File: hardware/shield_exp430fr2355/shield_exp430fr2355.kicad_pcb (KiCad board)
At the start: 2 copper layers, 78.4 x 50 mm, 50 parts, among them J1 TI_BOOSTER_40_J1, J10 Conn_01x02_Male, J12 Conn_01x02_Male, J13 Conn_01x02_Male, J14 Conn_01x02_Male, J15 Conn_01x02_Male, J16 Conn_01x02_Male, J17 Conn_01x02_Male, J18 Conn_01x02_Male, J19 Conn_01x02_Male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

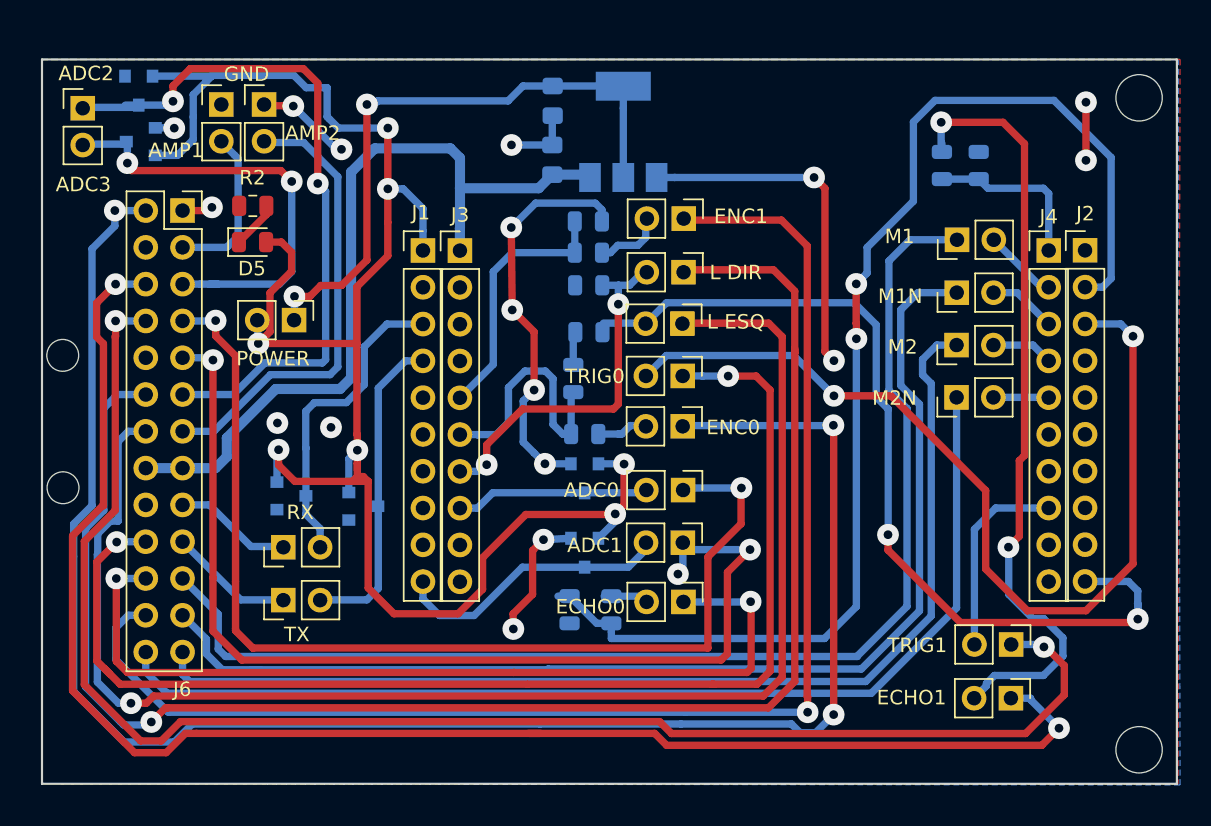
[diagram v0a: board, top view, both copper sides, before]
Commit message: Adicionado exemplo do ADC com trigger por timer.
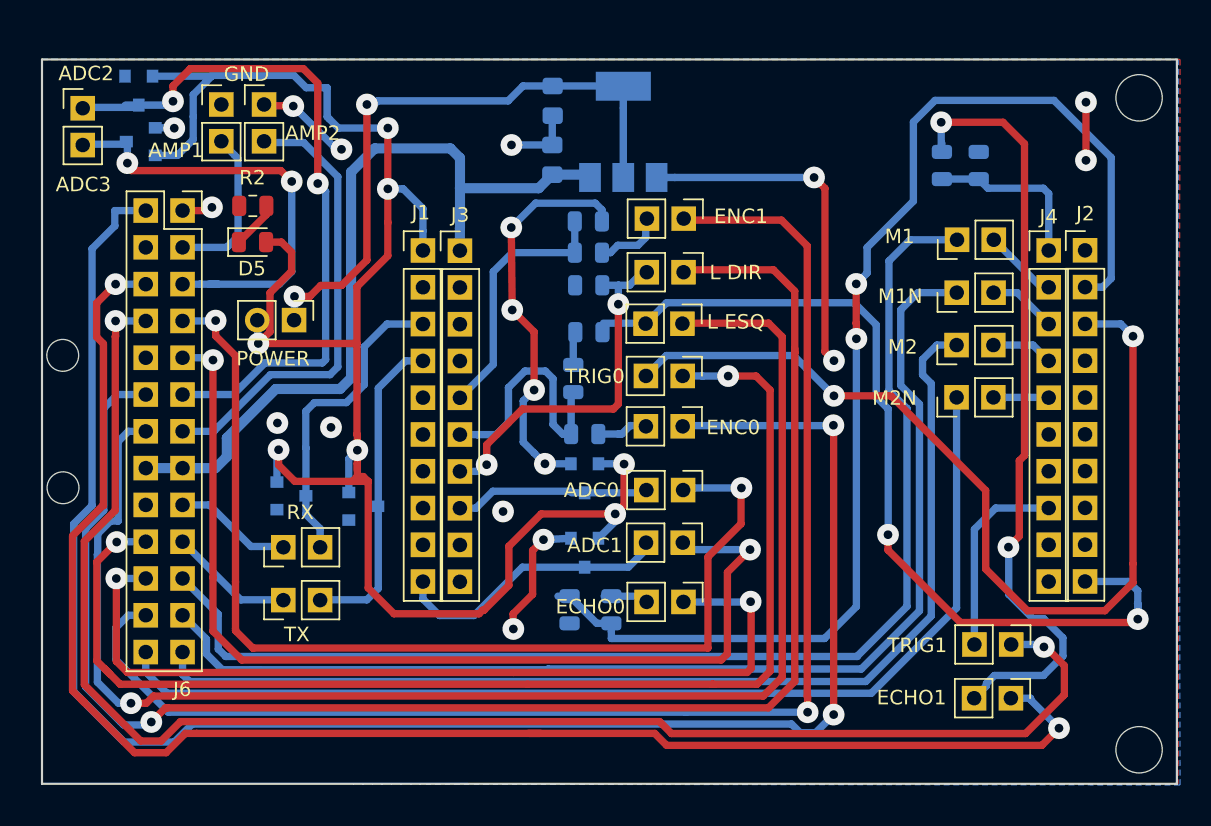
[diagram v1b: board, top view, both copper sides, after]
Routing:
- net ADC1: track 71.7 -> 69.9 mm, vias 3 -> 2
- net P2.2: track 65.4 -> 66.2 mm
- net D0: track 122.1 -> 122.0 mm, vias 3 -> 2
- net GND: vias 17 -> 18

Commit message: Added aligment info
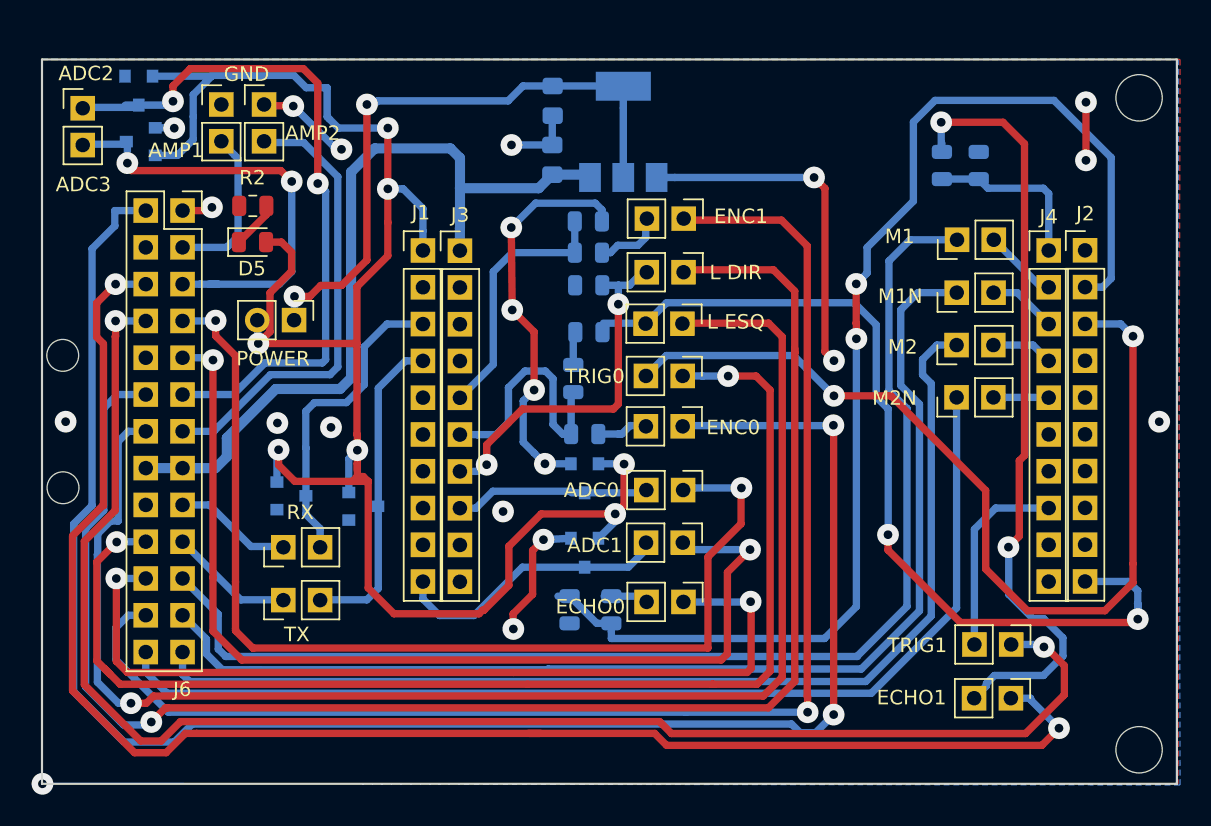
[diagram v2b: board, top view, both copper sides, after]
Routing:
- net GND: vias 18 -> 20
- net (no net): vias 0 -> 1
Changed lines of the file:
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@@
   (general
     (thickness 1.6)
-    (drawings 28)
-    (tracks 626)
+    (drawings 31)
+    (tracks 629)
     (zones 0)
     (modules 50)
@@
     (pad_to_mask_clearance 0)
     (solder_mask_min_width 0.25)
-    (aux_axis_origin 0 0)
+    (aux_axis_origin 171.1 172.9)
     (visible_elements 7FFFFFFF)
     (pcbplotparams
@@
       (padsonsilk false)
       (subtractmaskfromsilk false)
-      (outputformat 3)
+      (outputformat 1)
       (mirror false)
       (drillshape 0)
@@
     )
   )
+  (target plus (at 172.7 147.9) (size 2) (width 0.14986) (layer Edge.Cuts))
+  (target plus (at 248.2 147.9) (size 2) (width 0.14986) (layer Edge.Cuts))
+  (dimension 25.000799 (width 0.25) (layer F.SilkS)
+    (gr_text "25.001 mm" (at 261.2 135.400399 270) (layer F.SilkS)
+      (effects (font (size 1 1) (thickness 0.25)))
+    )
+    (feature1 (pts (xy 249.4 147.900799) (xy 260.286421 147.900799)))
+    (feature2 (pts (xy 249.4 122.9) (xy 260.286421 122.9)))
+    (crossbar (pts (xy 259.7 122.9) (xy 259.7 147.900799)))
+    (arrow1a (pts (xy 259.7 147.900799) (xy 259.113579 146.774295)))
+    (arrow1b (pts (xy 259.7 147.900799) (xy 260.286421 146.774295)))
+    (arrow2a (pts (xy 259.7 122.9) (xy 259.113579 124.026504)))
+    (arrow2b (pts (xy 259.7 122.9) (xy 260.286421 124.026504)))
+  )
+  (dimension 50.000899 (width 0.25) (layer F.SilkS)
+    (gr_text "50.001 mm" (at 256.3 147.900449 270) (layer F.SilkS)
+      (effects (font (size 1 1) (thickness 0.25)))
+    )
+    (feature1 (pts (xy 249.4 172.900899) (xy 255.386421 172.900899)))
+    (feature2 (pts (xy 249.4 122.9) (xy 255.386421 122.9)))
+    (crossbar (pts (xy 254.8 122.9) (xy 254.8 172.900899)))
+    (arrow1a (pts (xy 254.8 172.900899) (xy 254.213579 171.774395)))
+    (arrow1b (pts (xy 254.8 172.900899) (xy 255.386421 171.774395)))
+    (arrow2a (pts (xy 254.8 122.9) (xy 254.213579 124.026504)))
+    (arrow2b (pts (xy 254.8 122.9) (xy 255.386421 124.026504)))
+  )
   (gr_text M2N (at 229.92 146.27) (layer F.SilkS)
     (effects (font (size 1 1) (thickness 0.1)))
@@
     (arrow2b (pts (xy 189.765054 122.89217) (xy 190.351474 124.018673)))
   )
-  (dimension 50.8 (width 0.25) (layer Dwgs.User)
-    (gr_text "2.0000 in" (at 220.245053 115.542172) (layer Dwgs.User)
-      (effects (font (size 1 1) (thickness 0.25)))
-    )
-    (feature1 (pts (xy 245.645053 122.89217) (xy 245.645053 114.542172)))
-    (feature2 (pts (xy 194.845053 122.89217) (xy 194.845053 114.542172)))
-    (crossbar (pts (xy 194.845053 116.542172) (xy 245.645053 116.542172)))
-    (arrow1a (pts (xy 245.645053 116.542172) (xy 244.51855 117.128592)))
-    (arrow1b (pts (xy 245.645053 116.542172) (xy 244.51855 115.955752)))
-    (arrow2a (pts (xy 194.845053 116.542172) (xy 195.971556 117.128592)))
-    (arrow2b (pts (xy 194.845053 116.542172) (xy 195.971556 115.955752)))
-  )
   (gr_line (start 171.069 172.8978) (end 171.069 122.8852) (angle 90) (layer Edge.Cuts) (width 0.14986))
   (gr_line (start 249.42 122.90217) (end 249.42 172.9) (angle 90) (layer Edge.Cuts) (width 0.14986))
+  (via (at 171.1 172.9) (size 1.5) (drill 0.6) (layers F.Cu B.Cu) (net 0))
   (via (at 180.1996 127.635) (size 1.5) (drill 0.6) (layers F.Cu B.Cu) (net 1))
   (segment (start 178.8889 127.6121) (end 180.1767 127.6121) (width 0.508) (layer B.Cu) (net 1))
@@
   (segment (start 205.7908 150.8064) (end 205.2762 150.8064) (width 0.508) (layer F.Cu) (net 1))
   (via (at 205.7908 150.8064) (size 1.5) (drill 0.6) (layers F.Cu B.Cu) (net 1))
+  (via (at 172.7 147.9) (size 1.5) (drill 0.6) (layers F.Cu B.Cu) (net 1))
+  (via (at 248.2 147.9) (size 1.5) (drill 0.6) (layers F.Cu B.Cu) (net 1))
   (segment (start 205.36103 131.78217) (end 206.2988 130.8444) (width 0.7) (layer B.Cu) (net 2))
   (segment (start 199.925053 131.78217) (end 205.36103 131.78217) (width 0.7) (layer B.Cu) (net 2))

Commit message: Updated FR2553 PCB. Vias are now 1.8mm
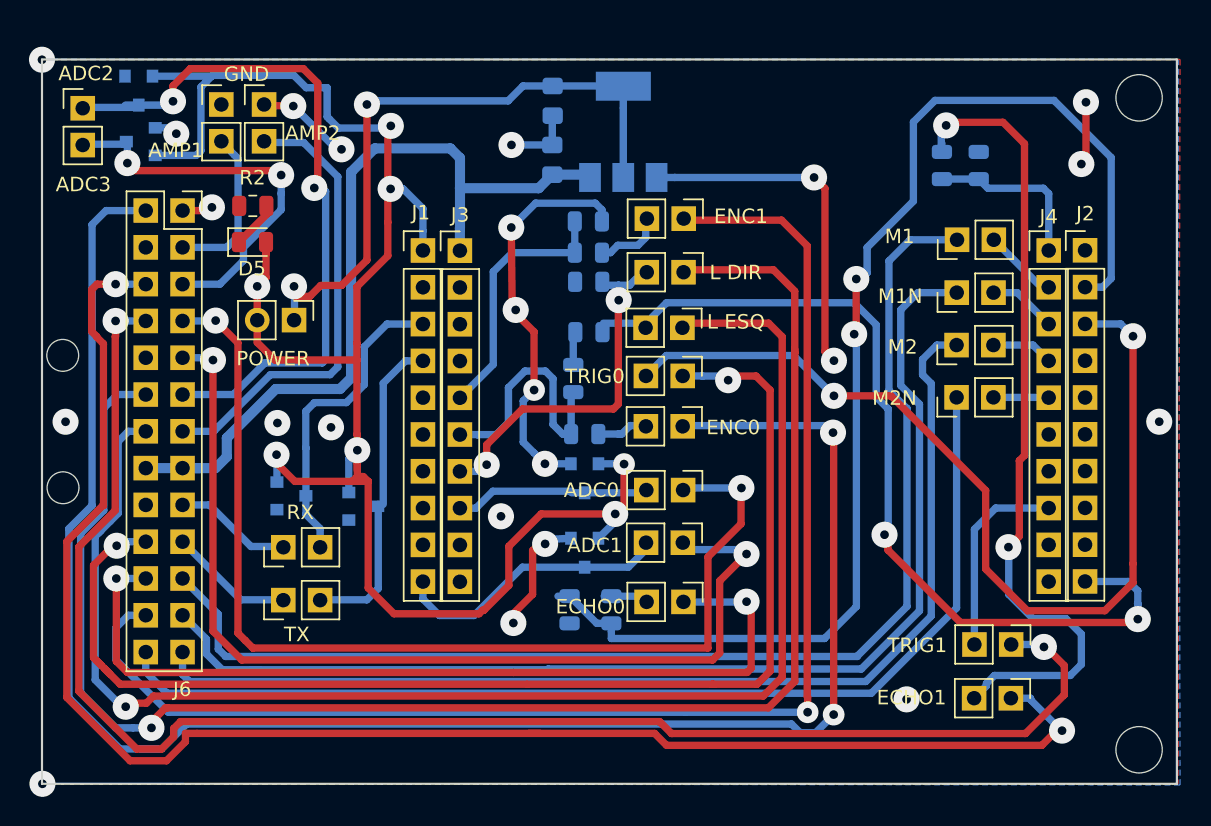
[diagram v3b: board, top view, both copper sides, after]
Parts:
- moved J25 0.28 mm to (215.3, 141.4)
- moved R8 0.24 mm to (208.8, 138.2)
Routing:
- net ADC3: track 31.3 -> 27.4 mm
- net Net-(J19-Pad2): track 54.3 -> 57.3 mm
- net Echo1: track 108.5 -> 110.8 mm
- net Trig1: track 105.5 -> 107.1 mm
- net +3V3: track 128.2 -> 126.6 mm
- net D0: track 122.0 -> 123.5 mm
- net R_TCRT: track 110.0 -> 111.0 mm
- net ADC1: track 69.9 -> 69.1 mm
- net Trig0: track 84.8 -> 85.4 mm
- net (no net): vias 1 -> 3
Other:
- net class +5V: via_dia 1.5 -> 1.8
- net class Default: via_dia 1.5 -> 1.8

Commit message: Updated FR2553 PCB. Connector pads are now 2x2mm
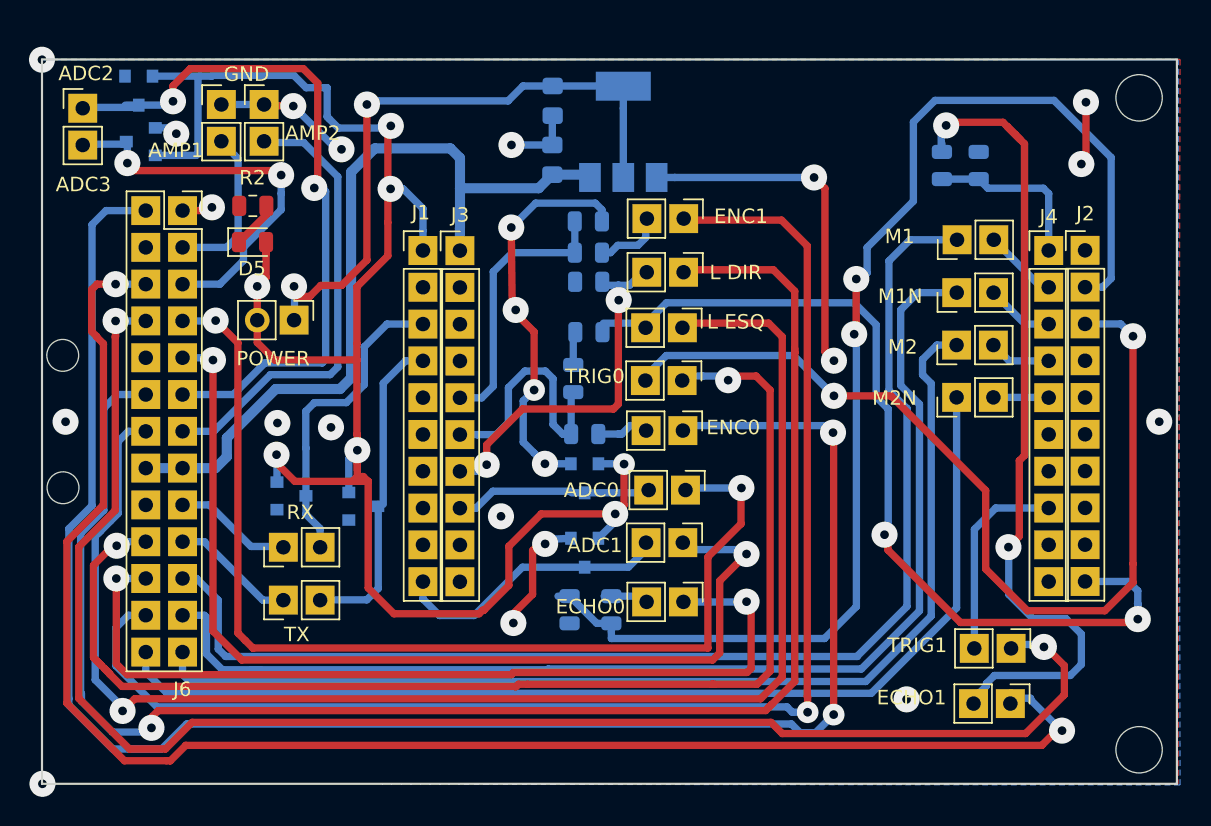
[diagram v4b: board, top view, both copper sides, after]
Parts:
- moved J19 0.37 mm to (237.9, 167.4)
- moved J14 0.32 mm to (215.3, 145.1)
- moved J22 0.29 mm to (215.3, 148.5)
- moved J20 0.27 mm to (238.0, 163.6)
- moved J12 0.16 mm to (215.5, 152.6)
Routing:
- net GND: track 82.6 -> 85.5 mm
- net Echo1: track 110.8 -> 109.2 mm
- net R_TCRT: track 111.0 -> 112.5 mm
- net Net-(J19-Pad2): track 57.3 -> 58.6 mm
- net PWM1N: track 81.9 -> 82.8 mm
- net P5.1: track 18.0 -> 18.9 mm
- net L_TCRT: track 99.2 -> 100.0 mm
- net PWM1: track 84.8 -> 85.3 mm
